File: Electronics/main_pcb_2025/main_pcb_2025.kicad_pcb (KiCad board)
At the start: 2 copper layers, 77.5 x 89 mm, 68 parts, among them J1 PI40HAT, J10 Conn_01x02_Male, J11 Conn_01x02_Male, J12 Conn_01x02_Male, J13 Conn_01x02_Male, J14 Conn_01x04_Male, J15 Conn_01x02_Male, J16 Conn_01x02_Male, J17 Conn_01x03_Male, J18 Conn_01x03_Male, J19 Conn_01x04_Male, J2 Conn_01x02_Male, J20 Conn_01x05, J21 Conn_01x05, J22 Conn_01x05, J23 22-03-5035, J24 Conn_01x02_Male, J25 Conn_01x02_Male, J26 Conn_01x02_Male, J27 Conn_01x02_Male, J3 Conn_01x02_Male, J4 Conn_01x02_Male, J5 Conn_01x02_Male, J6 Conn_01x02_Male, J7 Conn_01x04_Male, J8 Conn_01x02_Male, J9 22-03-5035, P1 R-78Bxx-2.0, P2 Amazon 10A stepdown, Q1 NVTR4503NT1G, Q2 NVTR4503NT1G, Q3 NVTR4503NT1G, Q4 NVTR4503NT1G, Q5 NVTR4503NT1G, Q6 NVTR4503NT1G, Q7 NVTR4503NT1G, Q8 NVTR4503NT1G, U1 SN74LVC1G125DBVR, U2 SN74LVC1G04DBVR, U4 Pololu_MAX14870, U6 Pololu_MAX14870, U7 SN74AHCT1G126DBVR, U8 PCA9635

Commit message: Update main robot PCB
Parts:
- removed D1, D2: LED, LED_THT:LED_D3.0mm
- removed J19: Conn_01x04_Male, Connector_JST:JST_SH_SM04B-SRSS-TB_1x04-1MP_P1.00mm_Horizontal
- removed P1: R-78Bxx-2.0, MiAM:CONV_R-78Bxx-2.0
- removed P2: Amazon 10A stepdown, MiAM:StepDown10A
- removed R2, R3: R, Resistor_SMD:R_0805_2012Metric
- added IC1: PCA9546AD, MiAM:SOIC127P600X175-16N, F.Cu at (92.8, 77.5)
- added J28: 9801-0-15-15-23-27-10-0, MiAM:9801015152327100, F.Cu at (115.0, 118.7)
- added J29: 9801-0-15-15-23-27-10-0, MiAM:9801015152327100, F.Cu at (109.0, 118.7)
- added J30: 9801-0-15-15-23-27-10-0, MiAM:9801015152327100, F.Cu at (121.0, 118.7)
- added J31: 22-03-5035, MiAM:SHDR3W60P0X250_1X3_990X490X590P, F.Cu at (100.7, 110.8)
- added J32: 22-03-5035, MiAM:SHDR3W60P0X250_1X3_990X490X590P, F.Cu at (100.7, 105.4)
- added J33: Conn_01x04_Male, Connector_JST:JST_SH_SM04B-SRSS-TB_1x04-1MP_P1.00mm_Horizontal, F.Cu at (127.5, 60.3)
- added R1: 10k, Resistor_SMD:R_0805_2012Metric, B.Cu at (103.2, 85.5)
- added R11: 4k, Resistor_SMD:R_0805_2012Metric, F.Cu at (97.7, 80.8)
- added RN3: EXB-2HV473JV, MiAM:EXB2HV_1, F.Cu at (110.8, 81.5)
- J14: value Conn_01x04_Male -> Conn_01x02_Pin; footprint Connector_JST:JST_SH_SM04B-SRSS-TB_1x04-1MP_P1.00mm_Horizontal -> MiAM:PogoPin_2.54
- J17, J18, JP1, JP2, R6: moved to B.Cu
- J2, J3, J4: value Conn_01x02_Male -> 9801-0-15-15-23-27-10-0; footprint MiAM:XT30UM -> MiAM:9801015152327100
- J20, J21, J22: value Conn_01x05 -> Conn_01x04_Male; footprint Connector_PinHeader_2.54mm:PinHeader_1x05_P2.54mm_Vertical -> Connector_JST:JST_SH_SM04B-SRSS-TB_1x04-1MP_P1.00mm_Horizontal
- RN1: value 47k -> EXB-2HV472JV; footprint Resistor_THT:R_Array_SIP9 -> MiAM:EXB2HV_1
- moved U8 102.8 mm to (102.5, 83.7), turned to 180 degrees
- moved RN1 101.1 mm to (97.5, 74.5), turned to 0 degrees
- moved RN2 91.2 mm to (108.2, 81.3), turned to -90 degrees
- moved D4 87.3 mm to (104.7, 70.9)
- moved J7 84.5 mm to (96.3, 60.3), turned to 180 degrees
- moved Q2 84.4 mm to (101.7, 75.8), turned to 90 degrees
- moved C1 82.9 mm to (114.8, 81.0), turned to 180 degrees
- moved D5 81.6 mm to (110.5, 70.9)
- moved Q3 80.9 mm to (105.2, 75.8), turned to 90 degrees
- moved C2 78.6 mm to (120.1, 81.0), turned to 180 degrees
- moved Q4 77.6 mm to (108.7, 75.8), turned to 90 degrees
- moved D6 76.8 mm to (115.5, 70.9)
- moved J11 76.4 mm to (102.8, 67.9)
- moved Q5 74.6 mm to (112.2, 75.8), turned to 90 degrees
- moved SPI0 72.6 mm to (135.2, 80.8), turned to 90 degrees
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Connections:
- J1 pad 12: /Servo DIR -> unconnected-(J1-BCM18-Pad12)
- J14 pad 1: GND -> /I2C SCL
- J14 pad 2: +3.3V -> /I2C SDA
- J2 pad 1: Net-(J2-Pin_1) -> +7.5V
- J20 pad 1: +3.3V -> GND
- J20 pad 2: GND -> +3.3V
- J20 pad 3: /I2C SCL -> /SDA0
- J20 pad 4: /I2C SDA -> /SCL0
- J21 pad 1: +3.3V -> GND
- J21 pad 2: GND -> +3.3V
- J21 pad 3: /I2C SCL -> /SDA2
- J21 pad 4: /I2C SDA -> /SCL2
- J22 pad 1: +3.3V -> GND
- J22 pad 2: GND -> +3.3V
- J22 pad 3: /I2C SCL -> /SDA1
- J22 pad 4: /I2C SDA -> /SCL1
- J3 pad 1: Net-(J2-Pin_1) -> +12V
- J4 pad 1: Net-(J2-Pin_2) -> +5V
- JP1 pad 2: /TX_EN -> /A0
- JP1 pad 3: /Servo DIR -> GND
- RN1 pad 1: GND -> /SDA0
- RN1 pad 2: /S7 -> /SCL0
- RN1 pad 3: /S6 -> /SDA1
- RN1 pad 4: /S5 -> /SCL1
- RN1 pad 5: /S4 -> /SDA2
- RN1 pad 6: /S3 -> /SCL2
- RN1 pad 7: /S2 -> /SDA3
- RN1 pad 8: /S1 -> unconnected-(RN1-Pad8)
- RN1 pad 9: /S0 -> +3.3V
- U2 pad 4: Net-(JP1-A) -> /TX_EN
- U8 pad 24: GND -> +3.3V
- U8 pad 25: GND -> +3.3V
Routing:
- net /SPI0 CLK: track 109.6 -> 0.00 mm, vias 3 -> 0
- net /SPI0 MISO: track 107.5 -> 0.00 mm, vias 3 -> 0
- net /SPI0 MOSI: track 104.9 -> 0.00 mm, vias 2 -> 0
- net /I2C SCL: track 91.9 -> 0.00 mm, vias 5 -> 0
- net /SPI0_CS1: track 87.2 -> 0.00 mm, vias 2 -> 0
- net /I2C SDA: track 87.2 -> 0.00 mm, vias 5 -> 0
- net +5V: track 65.9 -> 0.00 mm, vias 2 -> 0
- net /GPIO 19: track 59.7 -> 0.00 mm, vias 2 -> 0
- net /GPIO 13: track 56.7 -> 0.00 mm, vias 2 -> 0
- net /UART_HalfDuplex: track 50.5 -> 0.00 mm, vias 1 -> 0
- net /GPIO 4: track 43.2 -> 0.00 mm, vias 2 -> 0
- net /GPIO 16: track 42.1 -> 0.00 mm, vias 2 -> 0
- net /SPI0_CS0: track 41.6 -> 0.00 mm, vias 2 -> 0
- net +24V: track 41.3 -> 0.00 mm
- net /GPIO 21: track 37.5 -> 0.00 mm, vias 2 -> 0
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- added copper zone on F.Cu, net +12V
- added copper zone on B.Cu, net +5V
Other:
- board size 77.5 x 89 mm -> 56.8 x 67.3 mm
- board text added: "12V"
- board text added: "7V"
- board text added: "Mot1"
- board text added: "Mot2"

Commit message: Update main PCB
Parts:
- removed C4: Conn_03x04, MiAM:Pin_Header_Straight_3x04_Pitch2.54mm
- removed J17, J18: Conn_01x03_Male, Connector_PinHeader_2.54mm:PinHeader_1x03_P2.54mm_Vertical
- added C3: Conn_03x06, MiAM:Pin_Header_Straight_3x06_Pitch2.54mm, F.Cu at (90.9, 84.0)
- added JP3: SolderJumper_3_Open, Jumper:SolderJumper-3_P1.3mm_Open_Pad1.0x1.5mm, B.Cu at (116.9, 98.9)
- added JP4: SolderJumper_3_Open, Jumper:SolderJumper-3_P1.3mm_Open_Pad1.0x1.5mm, B.Cu at (116.9, 105.9)
- I2C0: renamed from J20; footprint Connector_JST:JST_SH_SM04B-SRSS-TB_1x04-1MP_P1.00mm_Horizontal -> MiAM:JST_SH_SM04B-SRSS-TB_1x04-1MP_P1.00mm_Horizontal
- I2C1: renamed from J22; footprint Connector_JST:JST_SH_SM04B-SRSS-TB_1x04-1MP_P1.00mm_Horizontal -> MiAM:JST_SH_SM04B-SRSS-TB_1x04-1MP_P1.00mm_Horizontal
- I2C2: renamed from J21; footprint Connector_JST:JST_SH_SM04B-SRSS-TB_1x04-1MP_P1.00mm_Horizontal -> MiAM:JST_SH_SM04B-SRSS-TB_1x04-1MP_P1.00mm_Horizontal
- I2C3: renamed from J33; footprint Connector_JST:JST_SH_SM04B-SRSS-TB_1x04-1MP_P1.00mm_Horizontal -> MiAM:JST_SH_SM04B-SRSS-TB_1x04-1MP_P1.00mm_Horizontal
- I2C4: renamed from J7; footprint Connector_JST:JST_SH_SM04B-SRSS-TB_1x04-1MP_P1.00mm_Horizontal -> MiAM:JST_SH_SM04B-SRSS-TB_1x04-1MP_P1.00mm_Horizontal
- J24: footprint Connector_Molex:Molex_PicoBlade_53047-0210_1x02_P1.25mm_Vertical -> MiAM:Molex_PicoBlade_53047-0210_1x02_P1.25mm_Vertical
- MOT1: renamed from J8; footprint Connector_Molex:Molex_PicoBlade_53047-0210_1x02_P1.25mm_Vertical -> MiAM:Molex_PicoBlade_53047-0210_1x02_P1.25mm_Vertical
- MOT2: renamed from J10; footprint Connector_Molex:Molex_PicoBlade_53047-0210_1x02_P1.25mm_Vertical -> MiAM:Molex_PicoBlade_53047-0210_1x02_P1.25mm_Vertical
- O0: renamed from J13; footprint Connector_Molex:Molex_PicoBlade_53047-0210_1x02_P1.25mm_Vertical -> MiAM:Molex_PicoBlade_53047-0210_1x02_P1.25mm_Vertical
- O1: renamed from J11; footprint Connector_Molex:Molex_PicoBlade_53047-0210_1x02_P1.25mm_Vertical -> MiAM:Molex_PicoBlade_53047-0210_1x02_P1.25mm_Vertical
- O2: renamed from J12; footprint Connector_Molex:Molex_PicoBlade_53047-0210_1x02_P1.25mm_Vertical -> MiAM:Molex_PicoBlade_53047-0210_1x02_P1.25mm_Vertical
- O3: renamed from J15; footprint Connector_Molex:Molex_PicoBlade_53047-0210_1x02_P1.25mm_Vertical -> MiAM:Molex_PicoBlade_53047-0210_1x02_P1.25mm_Vertical
- O4: renamed from J16; footprint Connector_Molex:Molex_PicoBlade_53047-0210_1x02_P1.25mm_Vertical -> MiAM:Molex_PicoBlade_53047-0210_1x02_P1.25mm_Vertical
- O5: renamed from J25; footprint Connector_Molex:Molex_PicoBlade_53047-0210_1x02_P1.25mm_Vertical -> MiAM:Molex_PicoBlade_53047-0210_1x02_P1.25mm_Vertical
- O6: renamed from J26; footprint Connector_Molex:Molex_PicoBlade_53047-0210_1x02_P1.25mm_Vertical -> MiAM:Molex_PicoBlade_53047-0210_1x02_P1.25mm_Vertical
- O7: renamed from J27; footprint Connector_Molex:Molex_PicoBlade_53047-0210_1x02_P1.25mm_Vertical -> MiAM:Molex_PicoBlade_53047-0210_1x02_P1.25mm_Vertical
- moved U4 20.5 mm to (125.3, 99.9), turned to 180 degrees
- moved U6 18.7 mm to (121.7, 85.4), turned to 180 degrees
- moved R1 13.9 mm to (93.0, 76.1), turned to 90 degrees
- moved R6 12.0 mm to (101.8, 82.6)
- moved R11 11.9 mm to (94.5, 69.3), turned to 90 degrees
- moved JP2 11.6 mm to (101.8, 86.6)
- moved RN1 10.8 mm to (91.8, 65.2)
- moved JP1 9.94 mm to (92.9, 80.1), turned to -90 degrees
- moved Q8 5.81 mm to (121.3, 81.4)
- moved D8 4.74 mm to (122.3, 71.8)
- moved D7 4.54 mm to (115.7, 71.8)
- moved D6 3.71 mm to (111.9, 71.8)
- moved D5 3.61 mm to (107.0, 71.8)
- moved C2 2.85 mm to (117.4, 81.9)
- moved MOT2 2.50 mm to (102.2, 97.0), turned to 0 degrees
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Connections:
- C1 pad 1: /S0 -> /S3
- C1 pad 2: /S1 -> /S2
- C1 pad 3: /S2 -> /S1
- C1 pad 4: /S3 -> /S0
- C2 pad 1: /S4 -> /S7
- C2 pad 2: /S5 -> /S6
- C2 pad 3: /S6 -> /S5
- C2 pad 4: /S7 -> /S4
- RN1 pad 8: unconnected-(RN1-Pad8) -> /SCL3
- RN3 pad 1: /S0 -> /S7
- RN3 pad 2: /S1 -> /S6
- RN3 pad 3: /S2 -> /S5
- RN3 pad 4: /S3 -> /S4
- RN3 pad 5: /S4 -> /S3
- RN3 pad 6: /S5 -> /S2
- RN3 pad 7: /S6 -> /S1
- RN3 pad 8: /S7 -> /S0
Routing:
- net /GPIO 16: track 0.00 -> 71.3 mm, vias 0 -> 3
- net /I2C SCL: track 0.00 -> 69.7 mm, vias 0 -> 1
- net /I2C SDA: track 0.00 -> 69.2 mm, vias 0 -> 1
- net /GPIO 12: track 0.00 -> 68.6 mm, vias 0 -> 2
- net /SPI0 MISO: track 0.00 -> 64.5 mm, vias 0 -> 2
- net /SPI0 CLK: track 0.00 -> 63.5 mm, vias 0 -> 1
- net /SPI0 MOSI: track 0.00 -> 61.9 mm, vias 0 -> 2
- net /UART_HalfDuplex: track 0.00 -> 60.2 mm, vias 0 -> 1
- net /SPI0_CS1: track 0.00 -> 58.7 mm, vias 0 -> 1
- net /SPI0_CS0: track 0.00 -> 51.6 mm, vias 0 -> 2
- net /SDA3: track 0.00 -> 48.9 mm, vias 0 -> 3
- net /SCL3: track 0.00 -> 47.8 mm, vias 0 -> 3
- net /GPIO 19: track 0.00 -> 47.2 mm, vias 0 -> 1
- net /GPIO 13: track 0.00 -> 46.2 mm, vias 0 -> 1
- net /SCL2: track 0.00 -> 41.8 mm, vias 0 -> 3
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- added copper zone on In1.Cu, net +24V
- added copper zone on In1.Cu, net +5V
- added copper zone on In2.Cu, net +7.5V
- added copper zone on F.Cu, net GND
- removed copper zone on F.Cu, net +24V
- removed copper zone on B.Cu, net +5V
- removed copper zone on F.Cu, net +7.5V
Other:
- board size 56.8 x 67.3 mm -> 56 x 65.5 mm
- copper layers 2 -> 4
- board text added: "I2C"
- board text added: "SPI0.0"
- board text added: "SPI0.1"
- board text removed: "0"
- board text removed: "1"
- board text removed: "2"
- board text removed: "24 - 7"
- board text removed: "24V"
- board text removed: "26"
- board text removed: "27"
- board text removed: "3"
- board text removed: "3V3"
- board text removed: "4"
- board text removed: "5"
- board text removed: "6"
- board text removed: "7"
- board text removed: "7V5"
- board text removed: "Battery"
- board text removed: "Emergency"
- board text removed: "GND"
- board text removed: "MOT1"
- board text removed: "MOT2"
- board text removed: "Mot1"
- board text removed: "Mot2"
- board text removed: "SCL"
- board text removed: "SDA"
- board text removed: "Switch"

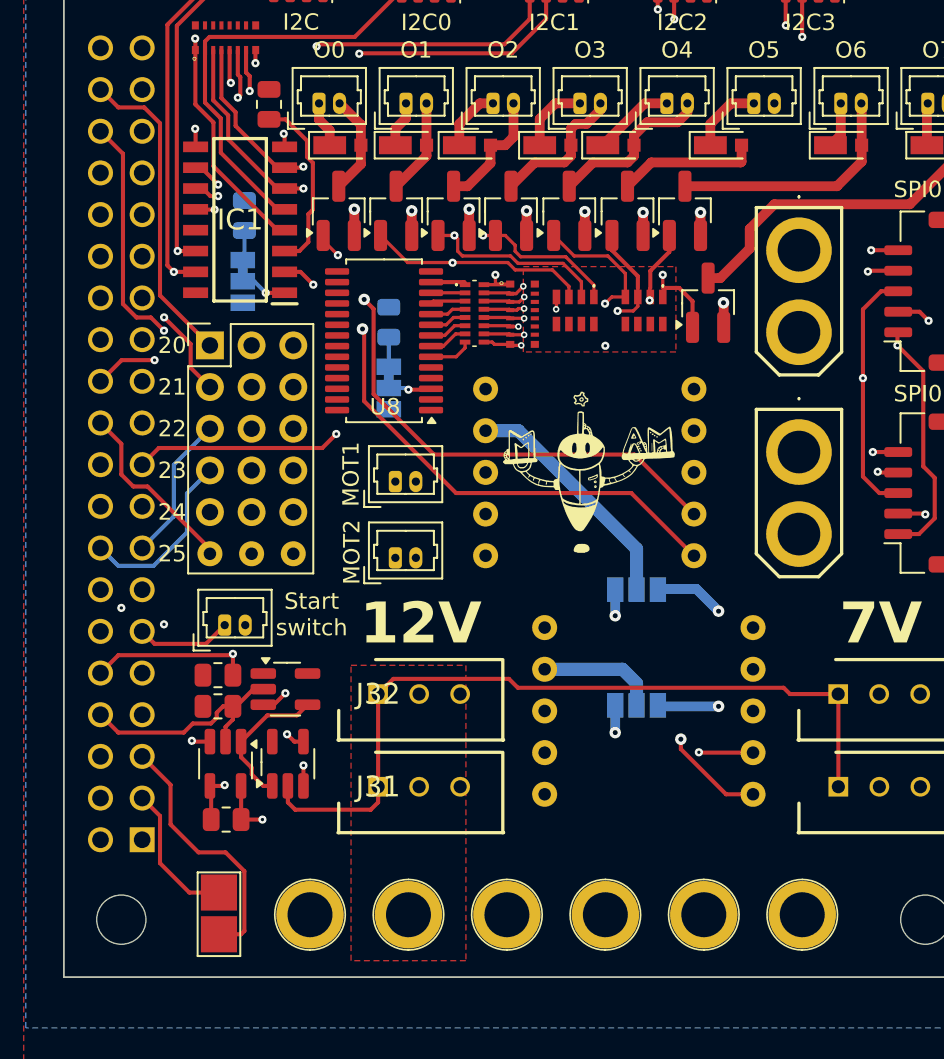
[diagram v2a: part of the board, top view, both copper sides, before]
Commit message: PCB update - passes DRC
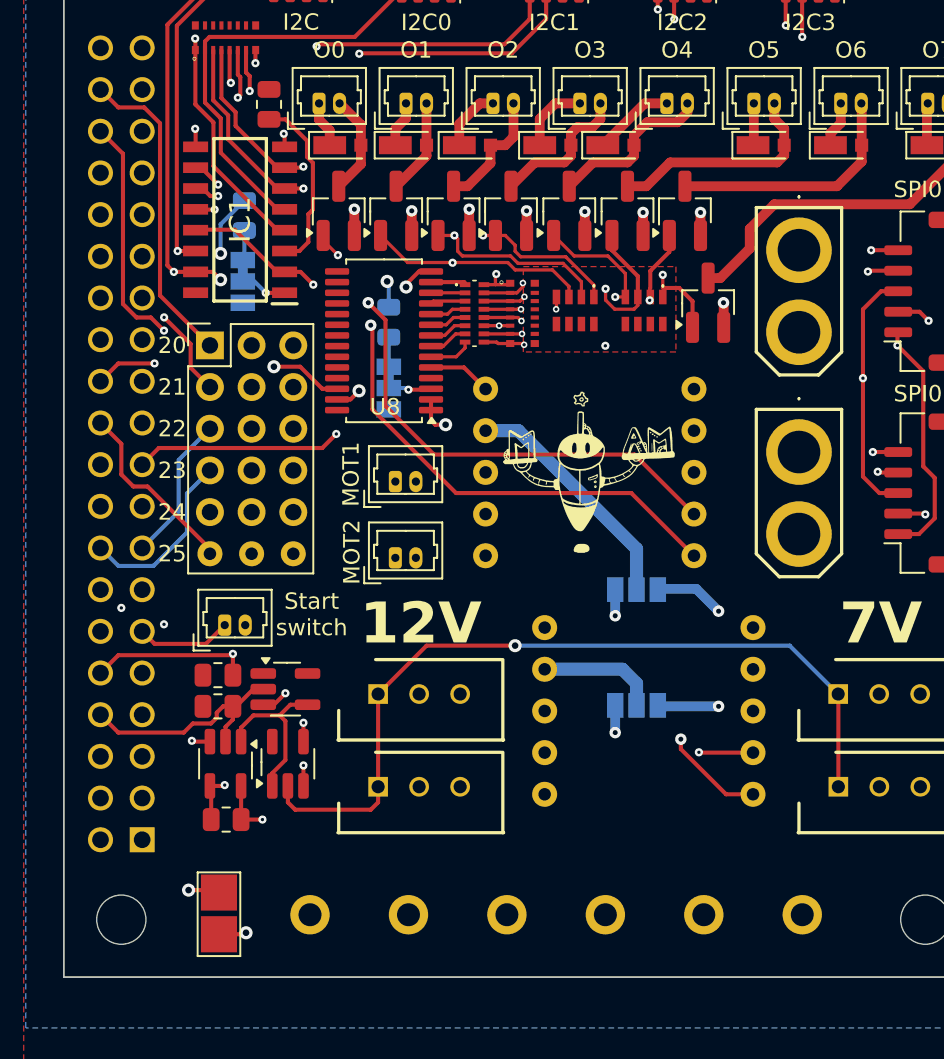
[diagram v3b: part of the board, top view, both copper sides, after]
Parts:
- J2, J28, J29, J3, J30, J4: value 9801-0-15-15-23-27-10-0 -> MilliMax0600; footprint MiAM:9801015152327100 -> MiAM:0600005150000
- moved J28 6.00 mm to (109.0, 118.7)
- moved J29 6.00 mm to (115.0, 118.7)
- moved D8 2.60 mm to (124.9, 71.8)
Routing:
- net Net-(MOT2-Pin_1): track 0.00 -> 15.6 mm
- net /I2C SDA: track 69.2 -> 84.0 mm, vias 1 -> 4
- net GND: track 29.3 -> 44.0 mm, vias 21 -> 23
- net Net-(MOT2-Pin_2): track 0.00 -> 12.6 mm
- net /I2C SCL: track 69.7 -> 78.6 mm, vias 1 -> 3
- net Net-(MOT1-Pin_1): track 0.00 -> 6.85 mm
- net +3.3V: track 0.00 -> 5.44 mm, vias 0 -> 2
- net Net-(D8-A): track 8.57 -> 13.7 mm
- net Net-(MOT1-Pin_2): track 0.00 -> 4.48 mm
- net +24V: track 31.8 -> 29.8 mm
- net /UART_HalfDuplex: track 60.2 -> 61.9 mm, vias 1 -> 2
- net /TX_EN: track 8.79 -> 10.3 mm
- net /SPI0_CS0: track 51.6 -> 52.9 mm
- net /S2: track 20.7 -> 19.5 mm
- net /S7: track 17.8 -> 17.0 mm
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- added copper zone on In2.Cu, net +12V
- removed copper zone on F.Cu, net +12V
